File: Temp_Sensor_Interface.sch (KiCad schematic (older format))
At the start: 4 parts, among them J15 Conn_01x03_Male

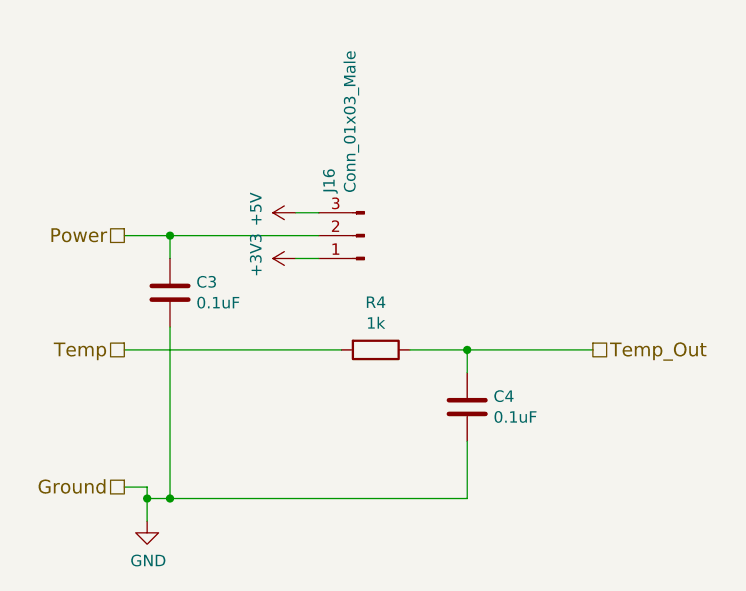
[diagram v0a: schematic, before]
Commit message: Pretty much ready to go. Should verify barrel jack first. Needs a logo.
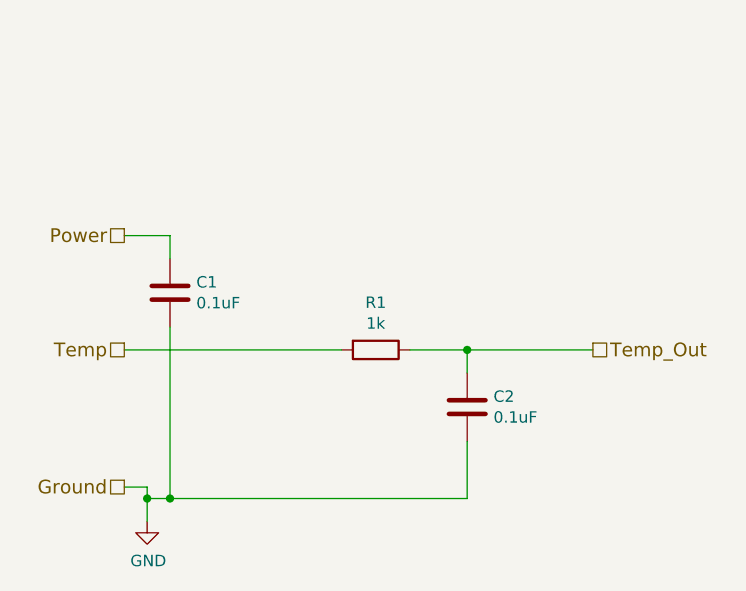
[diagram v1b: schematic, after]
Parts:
- removed J15: Conn_01x03_Male, Connectors:PINHEAD1-3, symbol Connector:Conn_01x03_Male
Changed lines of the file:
@@
 $Descr A4 11693 8268
 encoding utf-8
-Sheet 8 8
+Sheet 2 9
 Title ""
 Date ""
@@
 AR Path="/5A456F01/5A4A7604" Ref="R1"  Part="1"
 AR Path="/5A466974/5A4A7604" Ref="R4"  Part="1"
-F 0 "R4" V 3143 3050 50  0000 C CNN
+F 0 "R1" V 3143 3050 50  0000 C CNN
 F 1 "1k" V 3234 3050 50  0000 C CNN
 F 2 "Resistors_SMD:R_0805_HandSoldering" V 3280 3050 50  0001 C CNN
@@
 AR Path="/5A456F01/5A4A7684" Ref="C2"  Part="1"
 AR Path="/5A466974/5A4A7684" Ref="C4"  Part="1"
-F 0 "C4" H 3865 3346 50  0000 L CNN
+F 0 "C2" H 3865 3346 50  0000 L CNN
 F 1 "0.1uF" H 3865 3255 50  0000 L CNN
 F 2 "Capacitors_SMD:C_0805_HandSoldering" H 3788 3150 50  0001 C CNN
@@
 	1    3750 3300
 	1    0    0    -1
-$EndComp
-$Comp
-L power:+3V3 #PWR010
-U 1 1 5A4A7704
-P 3000 2650
-AR Path="/5A456F01/5A4A7704" Ref="#PWR010"  Part="1"
-AR Path="/5A466974/5A4A7704" Ref="#PWR014"  Part="1"
-F 0 "#PWR014" H 3000 2500 50  0001 C CNN
-F 1 "+3V3" H 3015 2823 50  0000 C CNN
-F 2 "" H 3000 2650 50  0001 C CNN
-F 3 "" H 3000 2650 50  0001 C CNN
-	1    3000 2650
-	0    -1   -1   0
 $EndComp
 $Comp
@@
 AR Path="/5A456F01/5A4A7B7F" Ref="C1"  Part="1"
 AR Path="/5A466974/5A4A7B7F" Ref="C3"  Part="1"
-F 0 "C3" H 2565 2846 50  0000 L CNN
+F 0 "C1" H 2565 2846 50  0000 L CNN
 F 1 "0.1uF" H 2565 2755 50  0000 L CNN
 F 2 "Capacitors_SMD:C_0805_HandSoldering" H 2488 2650 50  0001 C CNN
@@
 Wire Wire Line
 	2450 3700 2350 3700
-$Comp
-L Connector:Conn_01x03_Male J15
-U 1 1 5A4A85C7
-P 3300 2550
-AR Path="/5A456F01/5A4A85C7" Ref="J15"  Part="1"
-AR Path="/5A466974/5A4A85C7" Ref="J16"  Part="1"
-F 0 "J16" V 3453 2363 50  0000 R CNN
-F 1 "Conn_01x03_Male" V 3362 2363 50  0000 R CNN
-F 2 "Connectors:PINHEAD1-3" H 3300 2550 50  0001 C CNN
-F 3 "~" H 3300 2550 50  0001 C CNN
-	1    3300 2550
-	-1   0    0    1
-$EndComp
-$Comp
-L power:+5V #PWR09
-U 1 1 5A4A868C
-P 3000 2450
-AR Path="/5A456F01/5A4A868C" Ref="#PWR09"  Part="1"
-AR Path="/5A466974/5A4A868C" Ref="#PWR013"  Part="1"
-F 0 "#PWR013" H 3000 2300 50  0001 C CNN
-F 1 "+5V" H 3015 2623 50  0000 C CNN
-F 2 "" H 3000 2450 50  0001 C CNN
-F 3 "" H 3000 2450 50  0001 C CNN
-	1    3000 2450
-	0    -1   -1   0
-$EndComp
-Wire Wire Line
-	3000 2450 3100 2450
-Wire Wire Line
-	3100 2650 3000 2650
-Wire Wire Line
-	3100 2550 2450 2550
-Connection ~ 2450 2550
 Wire Wire Line
 	2250 2550 2450 2550
